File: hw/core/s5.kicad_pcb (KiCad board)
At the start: 4 copper layers, 131.5 x 100 mm, 236 parts, among them J10 SWD_2x3, J11 MC1,5/5-GF-3,5_1843826, J12 USB-C_2171820001, J2 LINK-PP_LPJG0926HENL, J3 LINK-PP_LPJG0926HENL, J4 LINK-PP_LPJG0926HENL, J5 LINK-PP_LPJG0926HENL, J6 LINK-PP_LPJG0926HENL, J7 Conn_01x03, J8 microSD, J9 Conn_02x06, K1 HFD23-024-1ZS, Q1 NMOS, Q2 NMOS, Q3 NMOS, Q4 NMOS, Q5 NMOS, Q60 2N7002, SW2 SW_Push, U1 KSZ9477S, U10 TPS3823, U11 TLV62569PDDCR, U12 AP2112K-1.8, U13 TPS23861, U15 DS18B20, U16 DS18B20, U17 SHT40-AD1B, U18 TPS7B6933QDCYRQ1, U19 STM32G071CBTx, U20 TPS7B6933QDCYRQ1, U21 EL357N, U3 AP2112K-2.5, U4 AP2112K-1.2, U7 T113-S3, U8 W25N02JWZEIF, U9 TPS23861, Y1 25MHz, Y2 24MHz, Y3 32.768kHz

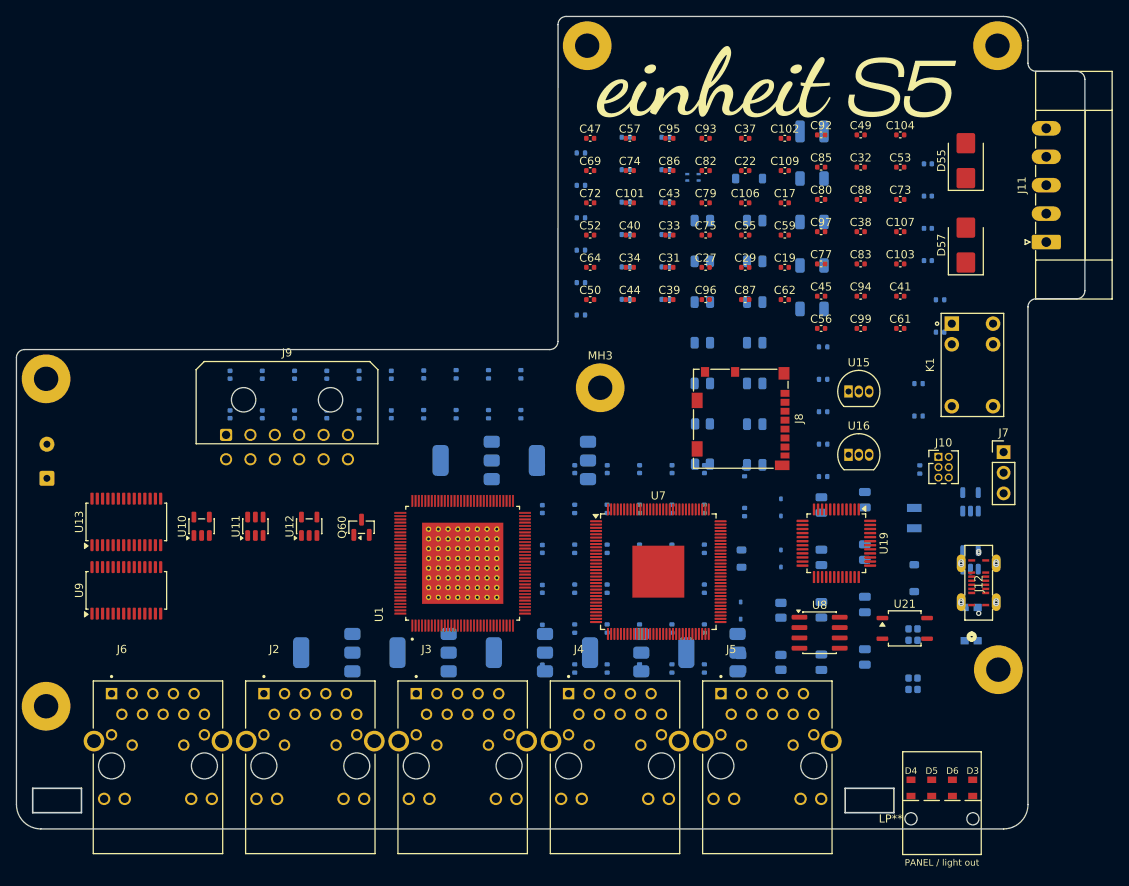
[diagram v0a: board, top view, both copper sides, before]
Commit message: s5-core: cap placement + routing progress; clear solder-mask bloat
Placed the remaining decoupling/bulk caps (one-per-pin per CAP_PLACEMENT.md) and
continued routing. Also cleared the easyeda 0.102mm solder_mask_margin bloat on
all 350 placed pads (KSZ U1 + magjacks J2-J6 + USB-C J12 + Phoenix J9) -> 0,
fixing the 'mask aperture bridges different nets' DRC errors on the KSZ.
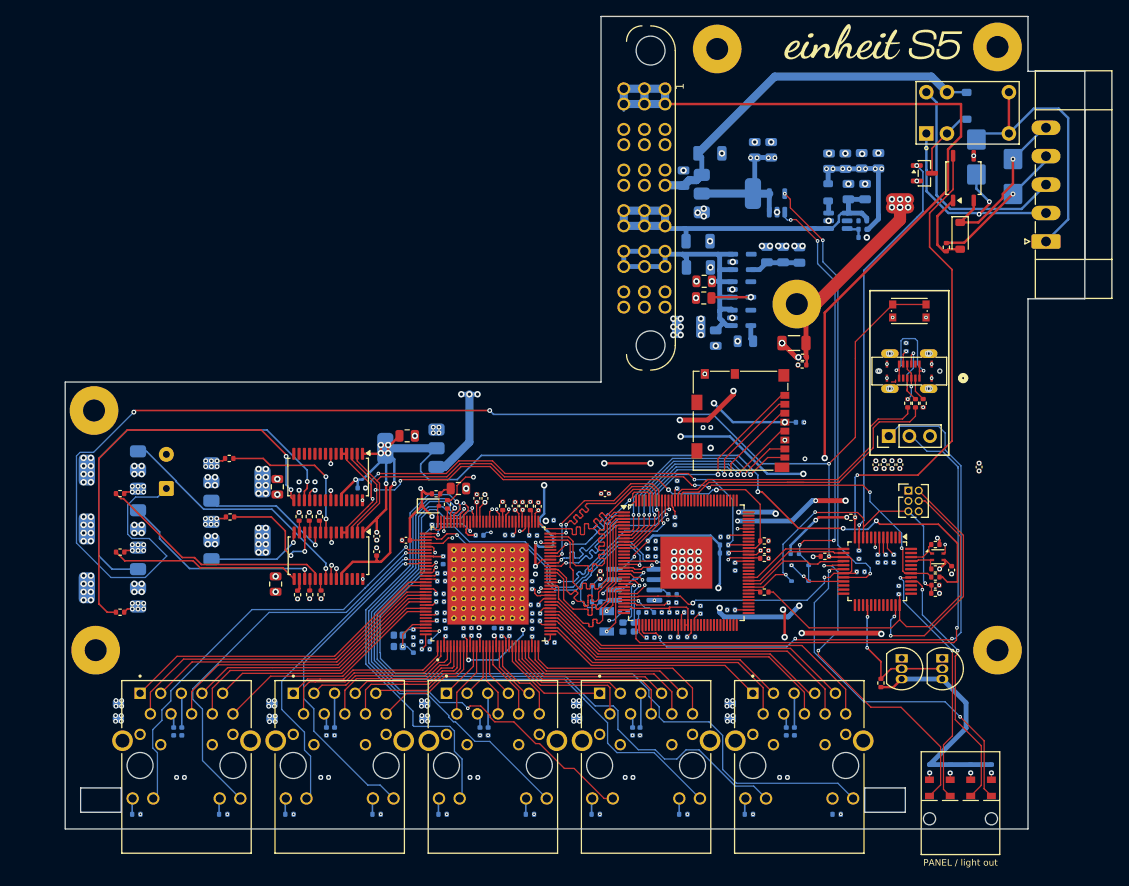
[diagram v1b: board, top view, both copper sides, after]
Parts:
- removed LP**: Mentor_1278.1004, Connector:Mentor_1278.1004_LightGuide
- removed the MH1 at (207.0, 57.6)
- removed the MH1 at (156.5, 57.6)
- removed the MH3 at (158.1, 99.7)
- removed the MH3 at (89.9, 98.6)
- added LP1: Mentor 1278.1004 4-way bargraph light guide, connectors:Mentor_1278.1004_LightGuide, F.Cu at (202.4, 148.9)
- added MH1: MountingHole_M2.5_PE, connectors:MountingHole_2.7mm_M2.5_6mmPad, F.Cu at (95.8, 102.5)
- added MH3: MountingHole_M2.5_PE, connectors:MountingHole_2.7mm_M2.5_6mmPad, F.Cu at (207.0, 57.8)
- added MH5: MountingHole_M2.5_PE, connectors:MountingHole_2.7mm_M2.5_6mmPad, F.Cu at (96.0, 132.0)
- added MH6: MountingHole_M2.5_PE, connectors:MountingHole_2.7mm_M2.5_6mmPad, F.Cu at (182.3, 89.4)
- C100, C108, C110, C13, C35, C36, C51, C63, C65, C68, C76, C91, D2, D56, R10, R12, R23, R25, R26, R28, R29, R31, R32, R34, R35, R36, R39, R42, R44, R48, R49, R5, R50, R55, R56, R58, R59, R6, R60, R61, R64, R65, R66, R67, R9, SW2, U17: moved to F.Cu
- C101, C102, C17, C19, C27, C29, C31, C32, C37, C38, C39, C40, C41, C43, C44, C45, C49, C50, C52, C53, C55, C56, C57, C59, C61, C69, C72, C73, C74, C77, C79, C80, C82, C83, C86, C87, C88, C92, C93, C94, C95, C96, C97, C99, D55, D57, U10, U11, U12, U8: moved to B.Cu
- J2, J3, J4, J5, J6: value LINK-PP_LPJG0926HENL -> LPJG0926HENL
- J9: value Conn_02x06 -> MPT-06-01-RA; footprint Connector_Molex:Molex_Micro-Fit_3.0_43045-1200_2x06_P3.00mm_Horizontal -> connectors:MPT-06-01-XX-X-RA-SD
- MH2, MH4: value MountingHole_M3_PE -> MountingHole_M2.5_PE; footprint MountingHole:MountingHole_3mm_Pad -> connectors:MountingHole_2.7mm_M2.5_6mmPad
- moved MH2 115.6 mm to (172.5, 58.0)
- moved C61 101.4 mm to (106.6, 142.0), turned to -90 degrees
- moved C73 100.4 mm to (124.2, 147.7)
- moved C53 98.3 mm to (125.4, 142.0), turned to -90 degrees
- moved R39 88.1 mm to (99.0, 127.3)
- moved R15 88.1 mm to (138.7, 152.2)
- moved R25 84.4 mm to (99.0, 119.9)
- moved R38 82.5 mm to (98.8, 139.5), turned to -90 degrees
- moved C49 82.4 mm to (135.1, 129.9), turned to -90 degrees
- moved Q60 81.8 mm to (198.0, 73.3), turned to 0 degrees
- moved U10 81.2 mm to (179.9, 77.0)
- moved U11 81.0 mm to (187.3, 79.2), turned to 0 degrees
- moved C78 80.4 mm to (161.7, 147.7), turned to 0 degrees
- moved C68 79.2 mm to (134.2, 118.5)
- moved Q2 77.1 mm to (98.1, 109.8)
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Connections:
- J9 pad 1: VBUS_54V -> MAIN_EN
- J9 pad 11: MAIN_EN -> GND
- J9 pad 2: GND -> MAIN_EN
- J9 pad 3: VBUS_54V -> MAIN_EN
- J9 pad 4: GND -> MAIN_EN
- J9 pad 5: VIN_24V -> MAIN_EN
- J9 pad 6: GND -> MAIN_EN
- J9 pad 7: VDD_5V -> GND
- J9 pad 9: VDD_3V3 -> GND
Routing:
- net VDD_3V3: track 0.00 -> 435.3 mm, vias 0 -> 43
- net SOC_RESET_N: track 0.00 -> 214.1 mm, vias 0 -> 7
- net VDD_1V2: track 0.00 -> 179.5 mm, vias 0 -> 25
- net VDD_2V5: track 0.00 -> 177.2 mm, vias 0 -> 15
- net VDD_3V3_PSE: track 0.00 -> 141.1 mm, vias 0 -> 11
- net VDD_3V3_SB: track 0.00 -> 126.1 mm, vias 0 -> 16
- net MAIN_EN: track 0.00 -> 125.7 mm, vias 0 -> 3
- net VDD_CORE: track 0.00 -> 121.3 mm, vias 0 -> 18
- net VDD_1V8: track 0.00 -> 104.4 mm, vias 0 -> 11
- net P4_YEL: track 0.00 -> 94.5 mm, vias 0 -> 1
- net PSE_RESET_N: track 0.00 -> 90.4 mm, vias 0 -> 4
- net U9_SRC12: track 0.00 -> 86.5 mm, vias 0 -> 10
- net P4_GRN: track 0.00 -> 86.5 mm, vias 0 -> 1
- net P3_YEL: track 0.00 -> 77.3 mm, vias 0 -> 1
- net U9_SRC8: track 0.00 -> 76.6 mm, vias 0 -> 10
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- added copper zone on In2.Cu, net PE
- added copper zone on In2.Cu, net VBUS_54V
- added copper zone on In2.Cu, net VDD_1V2
- added copper zone on In2.Cu, net VDD_1V8
- added copper zone on In2.Cu, net VDD_2V5
- added copper zone on In2.Cu, net VDD_3V3
- added copper zone on In2.Cu, net VDD_3V3_SB
- added copper zone on In2.Cu, net VDD_CORE
- added copper zone on In2.Cu, net VIN_24V
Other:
- board size 131.5 x 100 mm -> 125.5 x 100 mm
